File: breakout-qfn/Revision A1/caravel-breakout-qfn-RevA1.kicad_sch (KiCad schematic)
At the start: 14 parts, among them CON1 REF-182665-01, CON2 REF-182665-01, CON3 73251-1352, U1 Caravel, U2 TLV73318PDBV

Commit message: WIP checkin for comments
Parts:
- removed U1: Caravel, ok-chips:Caravel_WLCSP, symbol ok-chips:Caravel_WLCSP
- added U1: Caravel_QFN, Package_DFN_QFN:QFN-64-1EP_9x9mm_P0.5mm_EP7.65x7.65mm, symbol ok-chips:Caravel_QFN
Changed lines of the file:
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@@
     )
-  )
-  (symbol (lib_id "ok-chips:Caravel_WLCSP") (at 93.98 82.55 90) (unit 1)
-    (in_bom yes) (on_board yes)
-    (property "Reference" "U1" (id 0) (at 64.77 54.61 90)
-      (effects (font (size 1.27 1.27)) (justify left))
-    )
-    (property "Value" "Caravel" (id 1) (at 134.62 107.95 90)
-      (effects (font (size 1.27 1.27)) (justify left))
-    )
-    (property "Footprint" "ok-chips:Caravel_WLCSP" (id 2) (at 137.16 54.61 0)
-      (effects (font (size 1.27 1.27)) (justify left) hide)
-    )
-    (property "Datasheet" "" (id 3) (at 93.98 82.55 0)
-      (effects (font (size 1.27 1.27)) hide)
-    )
-    (property "LibSource" "https://github.com/efabless/caravel_board/blob/84c2a618c3ccb63b4e827d80adff53c441349ad6/hardware/symbols/Caravel_board.kicad_sym" (id 4) (at 139.7 54.61 0)
-      (effects (font (size 1.27 1.27)) (justify left) hide)
-    )
-    (pin "A1")
-    (pin "A10")
-    (pin "A2")
-    (pin "A3")
-    (pin "A4")
-    (pin "A5")
-    (pin "A6")
-    (pin "A7")
-    (pin "A8")
-    (pin "A9")
-    (pin "B1")
-    (pin "B10")
-    (pin "B2")
-    (pin "B3")
-    (pin "B4")
-    (pin "B5")
-    (pin "B6")
-    (pin "B7")
-    (pin "B8")
-    (pin "B9")
-    (pin "C1")
-    (pin "C10")
-    (pin "C2")
-    (pin "C3")
-    (pin "C4")
-    (pin "C5")
-    (pin "C6")
-    (pin "C7")
-    (pin "C8")
-    (pin "C9")
-    (pin "D1")
-    (pin "D10")
-    (pin "D2")
-    (pin "D3")
-    (pin "D4")
-    (pin "D5")
-    (pin "D6")
-    (pin "D7")
-    (pin "D8")
-    (pin "D9")
-    (pin "E1")
-    (pin "E10")
-    (pin "E2")
-    (pin "E3")
-    (pin "E4")
-    (pin "E5")
-    (pin "E6")
-    (pin "E7")
-    (pin "E8")
-    (pin "E9")
-    (pin "F1")
-    (pin "F10")
-    (pin "F2")
-    (pin "F3")
-    (pin "F4")
-    (pin "F5")
-    (pin "F6")
-    (pin "F7")
-    (pin "F8")
-    (pin "F9")
   )
   (symbol (lib_id "Device:C") (at 162.56 69.85 0) (unit 1)
@@
     )
     (pin "1")
-  )
-  (symbol (lib_id "Regulator_Linear:TLV73318PDBV") (at 144.78 157.48 0) (unit 1)
-    (in_bom yes) (on_board yes) (fields_autoplaced)
-    (property "Reference" "U2" (id 0) (at 144.78 147.32 0))
-    (property "Value" "TLV73318PDBV" (id 1) (at 144.78 149.86 0))
-    (property "Footprint" "Package_TO_SOT_SMD:SOT-23-5" (id 2) (at 144.78 149.225 0)
-      (effects (font (size 1.27 1.27) italic) hide)
-    )
-    (property "Datasheet" "http://www.ti.com/lit/ds/symlink/tlv733p.pdf" (id 3) (at 144.78 157.48 0)
-      (effects (font (size 1.27 1.27)) hide)
-    )
-    (pin "1")
-    (pin "2")
-    (pin "3")
-    (pin "4")
-    (pin "5")
   )
   (symbol (lib_id "Connector_Generic:Conn_02x20_Odd_Even") (at 222.25 52.07 0) (unit 1)
@@
     (pin "9")
   )
+  (symbol (lib_id "Device:C") (at 161.29 156.21 180) (unit 1)
+    (in_bom yes) (on_board yes)
+    (property "Reference" "C9" (id 0) (at 157.48 156.21 90))
+    (property "Value" "0.1uf" (id 1) (at 154.94 156.21 90))
+    (property "Footprint" "Capacitor_SMD:C_0603_1608Metric" (id 2) (at 160.3248 152.4 0)
+      (effects (font (size 1.27 1.27)) hide)
+    )
+    (property "Datasheet" "~" (id 3) (at 161.29 156.21 0)
+      (effects (font (size 1.27 1.27)) hide)
+    )
+    (pin "1")
+    (pin "2")
+  )
+  (symbol (lib_id "Regulator_Linear:TLV73318PDBV") (at 146.05 154.94 0) (unit 1)
+    (in_bom yes) (on_board yes) (fields_autoplaced)
+    (property "Reference" "U2" (id 0) (at 146.05 144.78 0))
+    (property "Value" "TLV73318PDBV" (id 1) (at 146.05 147.32 0))
+    (property "Footprint" "Package_TO_SOT_SMD:SOT-23-5" (id 2) (at 146.05 146.685 0)
+      (effects (font (size 1.27 1.27) italic) hide)
+    )
+    (property "Datasheet" "http://www.ti.com/lit/ds/symlink/tlv733p.pdf" (id 3) (at 146.05 154.94 0)
+      (effects (font (size 1.27 1.27)) hide)
+    )
+    (pin "1")
+    (pin "2")
+    (pin "3")
+    (pin "4")
+    (pin "5")
+  )
   (symbol (lib_id "power:GND") (at 234.95 81.28 0) (unit 1)
     (in_bom yes) (on_board yes)
@@
     (pin "1")
   )
+  (symbol (lib_id "ok-chips:Caravel_QFN") (at 35.56 175.26 0) (unit 1)
+    (in_bom yes) (on_board yes) (fields_autoplaced)
+    (property "Reference" "U1" (id 0) (at 67.31 145.8212 0))
+    (property "Value" "Caravel_QFN" (id 1) (at 67.31 148.3612 0))
+    (property "Footprint" "Package_DFN_QFN:QFN-64-1EP_9x9mm_P0.5mm_EP7.65x7.65mm" (id 2) (at 60.96 209.55 0)
+      (effects (font (size 1.27 1.27)) (justify left) hide)
+    )
+    (property "Datasheet" "" (id 3) (at 35.56 175.26 0)
+      (effects (font (size 1.27 1.27)) hide)
+    )
+    (property "LibSource" "https://github.com/efabless/caravel_board/blob/84c2a618c3ccb63b4e827d80adff53c441349ad6/hardware/symbols/Caravel_board.kicad_sym" (id 4) (at 60.96 212.09 0)
+      (effects (font (size 1.27 1.27)) (justify left) hide)
+    )
+    (pin "1")
+    (pin "10")
+    (pin "11")
+    (pin "12")
+    (pin "13")
+    (pin "14")
+    (pin "15")
+    (pin "16")
+    (pin "17")
+    (pin "18")
+    (pin "19")
+    (pin "2")
+    (pin "20")
+    (pin "21")
+    (pin "22")
+    (pin "23")
+    (pin "24")
+    (pin "25")
+    (pin "26")
+    (pin "27")
+    (pin "28")
+    (pin "29")
+    (pin "3")
+    (pin "30")
+    (pin "31")
+    (pin "32")
+    (pin "33")
+    (pin "34")
+    (pin "35")
+    (pin "36")
+    (pin "37")
+    (pin "38")
+    (pin "39")
+    (pin "4")
+    (pin "40")
+    (pin "41")
+    (pin "42")
+    (pin "43")
+    (pin "44")
+    (pin "45")
+    (pin "46")
+    (pin "47")
+    (pin "48")
+    (pin "49")
+    (pin "5")
+    (pin "50")
+    (pin "51")
+    (pin "52")
+    (pin "53")
+    (pin "54")
+    (pin "55")
+    (pin "56")
+    (pin "57")
+    (pin "58")
+    (pin "59")
+    (pin "6")
+    (pin "60")
+    (pin "61")
+    (pin "62")
+    (pin "63")
+    (pin "64")
+    (pin "65")
+    (pin "7")
+    (pin "8")
+    (pin "9")
+  )
   (symbol (lib_id "power:GND") (at 212.09 81.28 0) (unit 1)
     (in_bom yes) (on_board yes)
@@
     (pin "1")
   )
-  (symbol (lib_id "Device:C") (at 129.54 158.75 180) (unit 1)
-    (in_bom yes) (on_board yes)
-    (property "Reference" "C8" (id 0) (at 125.73 158.75 90))
-    (property "Value" "0.1uf" (id 1) (at 123.19 158.75 90))
-    (property "Footprint" "Capacitor_SMD:C_0603_1608Metric" (id 2) (at 128.5748 154.94 0)
-      (effects (font (size 1.27 1.27)) hide)
-    )
-    (property "Datasheet" "~" (id 3) (at 129.54 158.75 0)
-      (effects (font (size 1.27 1.27)) hide)
-    )
-    (pin "1")
-    (pin "2")
-  )
   (symbol (lib_id "power:GND") (at 212.09 154.94 0) (unit 1)
     (in_bom yes) (on_board yes)
@@
     (pin "1")
   )
-  (symbol (lib_id "Device:C") (at 160.02 158.75 180) (unit 1)
-    (in_bom yes) (on_board yes)
-    (property "Reference" "C9" (id 0) (at 156.21 158.75 90))
-    (property "Value" "0.1uf" (id 1) (at 153.67 158.75 90))
-    (property "Footprint" "Capacitor_SMD:C_0603_1608Metric" (id 2) (at 159.0548 154.94 0)
-      (effects (font (size 1.27 1.27)) hide)
-    )
-    (property "Datasheet" "~" (id 3) (at 160.02 158.75 0)
+  (symbol (lib_id "Device:C") (at 130.81 156.21 180) (unit 1)
+    (in_bom yes) (on_board yes)
+    (property "Reference" "C8" (id 0) (at 127 156.21 90))
+    (property "Value" "0.1uf" (id 1) (at 124.46 156.21 90))
+    (property "Footprint" "Capacitor_SMD:C_0603_1608Metric" (id 2) (at 129.8448 152.4 0)
+      (effects (font (size 1.27 1.27)) hide)
+    )
+    (property "Datasheet" "~" (id 3) (at 130.81 156.21 0)
       (effects (font (size 1.27 1.27)) hide)
     )
@@
       (reference "C7") (unit 1) (value "0.1uf") (footprint "Capacitor_SMD:C_0402_1005Metric")
     )
-    (path "/748e673c-62ba-48f2-8c93-fcf00774af87"
+    (path "/a1f5d155-7c5b-450f-835a-1beaa84985c2"
       (reference "C8") (unit 1) (value "0.1uf") (footprint "Capacitor_SMD:C_0603_1608Metric")
     )
-    (path "/9c14b6d3-b2f0-4fdc-9232-d4338971c346"
+    (path "/490fa7a0-dc17-4ffe-be30-513cc3f5aca8"
       (reference "C9") (unit 1) (value "0.1uf") (footprint "Capacitor_SMD:C_0603_1608Metric")
     )
@@
       (reference "CON3") (unit 1) (value "73251-1352") (footprint "ok-connectors:TE_5-1814832-2")
     )
-    (path "/00000000-0000-0000-0000-0000612e097b"
-      (reference "U1") (unit 1) (value "Caravel") (footprint "ok-chips:Caravel_WLCSP")
-    )
-    (path "/0d29bb03-4b1f-4213-ba3c-74ea953f1fc4"
+    (path "/629c3e8d-0778-4ca7-bedf-2cc0e61e7e2f"
+      (reference "U1") (unit 1) (value "Caravel_QFN") (footprint "Package_DFN_QFN:QFN-64-1EP_9x9mm_P0.5mm_EP7.65x7.65mm")
+    )
+    (path "/54c9bf1d-870a-4c32-88f6-52ae382a86f1"
       (reference "U2") (unit 1) (value "TLV73318PDBV") (footprint "Package_TO_SOT_SMD:SOT-23-5")
     )

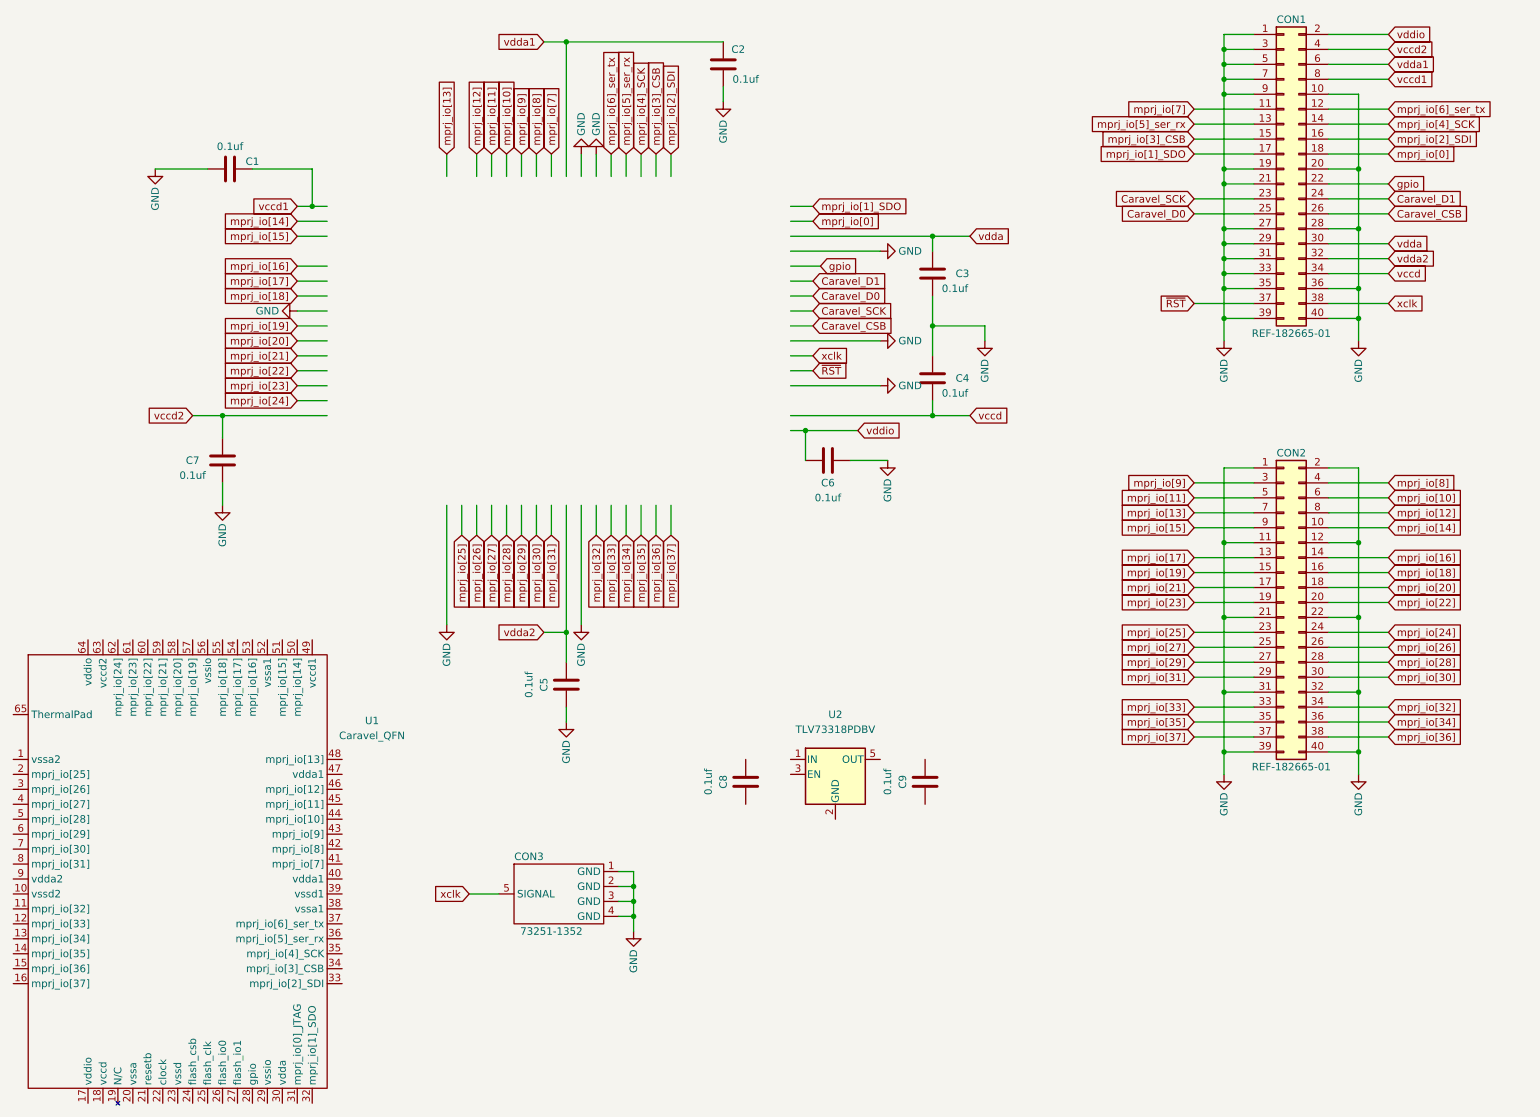
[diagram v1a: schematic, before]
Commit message: kicad 7 migration, qfn symbol and wiring
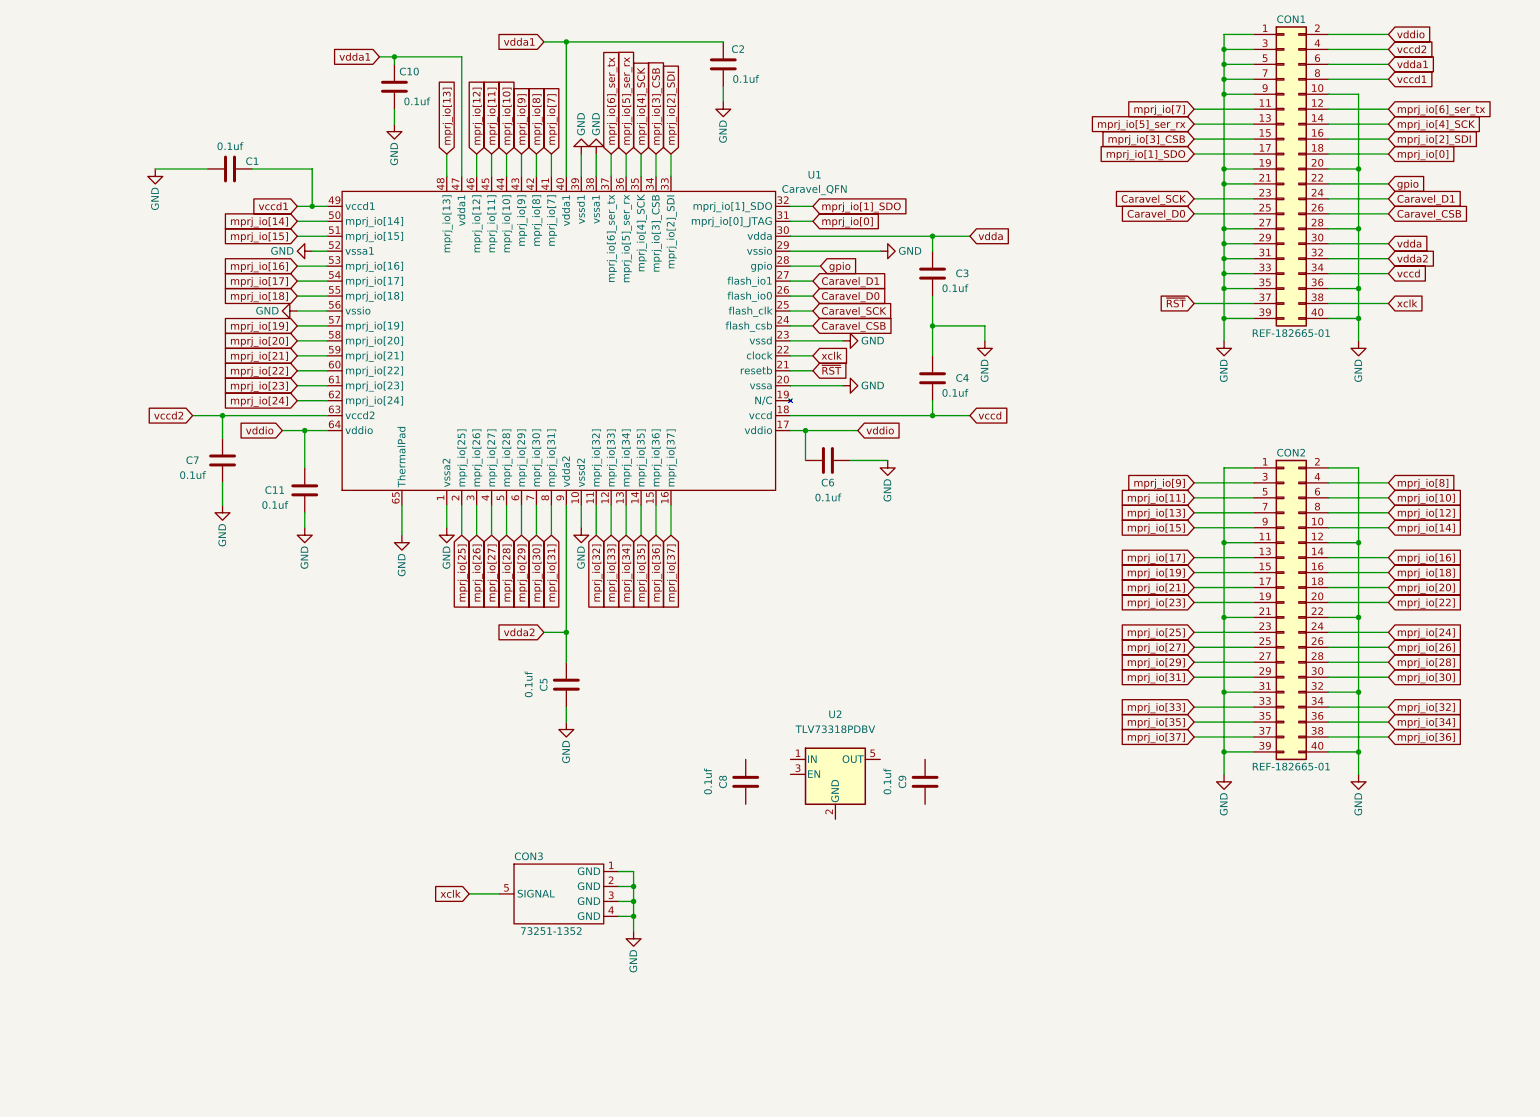
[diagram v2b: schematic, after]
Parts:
- removed U1: Caravel_QFN, Package_DFN_QFN:QFN-64-1EP_9x9mm_P0.5mm_EP7.65x7.65mm, symbol ok-chips:Caravel_QFN
- added C10, C11: 0.1uf, Capacitor_SMD:C_0402_1005Metric, symbol Device:C
- added U1: Caravel_QFN, Package_DFN_QFN:QFN-64-1EP_9x9mm_P0.5mm_EP7.65x7.65mm, symbol CaravelCommon:Caravel_QFN
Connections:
- net Caravel_CSB: now also U1.24 (flash_csb)
- net Caravel_D0: now also U1.26 (flash_io0)
- net Caravel_D1: now also U1.27 (flash_io1)
- net Caravel_SCK: now also U1.25 (flash_clk)
- net GND: now also C10.2, C11.1, U1.1 (vssa2), U1.10 (vssd2), U1.20 (vssa), U1.23 (vssd), U1.29 (vssio), U1.38 (vssa1), U1.39 (vssd1), U1.52 (vssa1), U1.56 (vssio), U1.65 (ThermalPad)
- net gpio: now also U1.28 (gpio)
- net mprj_io[0]: now also U1.31 (mprj_io[0]_JTAG)
- net mprj_io[10]: now also U1.44 (mprj_io[10])
- net mprj_io[11]: now also U1.45 (mprj_io[11])
- net mprj_io[12]: now also U1.46 (mprj_io[12])
- net mprj_io[13]: now also U1.48 (mprj_io[13])
- net mprj_io[14]: now also U1.50 (mprj_io[14])
- net mprj_io[15]: now also U1.51 (mprj_io[15])
- net mprj_io[16]: now also U1.53 (mprj_io[16])
- net mprj_io[17]: now also U1.54 (mprj_io[17])
- net mprj_io[18]: now also U1.55 (mprj_io[18])
- net mprj_io[19]: now also U1.57 (mprj_io[19])
- net mprj_io[1]_SDO: now also U1.32 (mprj_io[1]_SDO)
- net mprj_io[20]: now also U1.58 (mprj_io[20])
- net mprj_io[21]: now also U1.59 (mprj_io[21])
- net mprj_io[22]: now also U1.60 (mprj_io[22])
- net mprj_io[23]: now also U1.61 (mprj_io[23])
- net mprj_io[24]: now also U1.62 (mprj_io[24])
- net mprj_io[25]: now also U1.2 (mprj_io[25])
- net mprj_io[26]: now also U1.3 (mprj_io[26])
- net mprj_io[27]: now also U1.4 (mprj_io[27])
- net mprj_io[28]: now also U1.5 (mprj_io[28])
- net mprj_io[29]: now also U1.6 (mprj_io[29])
- net mprj_io[2]_SDI: now also U1.33 (mprj_io[2]_SDI)
- net mprj_io[30]: now also U1.7 (mprj_io[30])
- net mprj_io[31]: now also U1.8 (mprj_io[31])
- net mprj_io[32]: now also U1.11 (mprj_io[32])
- net mprj_io[33]: now also U1.12 (mprj_io[33])
- net mprj_io[34]: now also U1.13 (mprj_io[34])
- net mprj_io[35]: now also U1.14 (mprj_io[35])
- net mprj_io[36]: now also U1.15 (mprj_io[36])
- net mprj_io[37]: now also U1.16 (mprj_io[37])
- net mprj_io[3]_CSB: now also U1.34 (mprj_io[3]_CSB)
- net mprj_io[4]_SCK: now also U1.35 (mprj_io[4]_SCK)
- net mprj_io[5]_ser_rx: now also U1.36 (mprj_io[5]_ser_rx)
- net mprj_io[6]_ser_tx: now also U1.37 (mprj_io[6]_ser_tx)
- net mprj_io[7]: now also U1.41 (mprj_io[7])
- net mprj_io[8]: now also U1.42 (mprj_io[8])
- net mprj_io[9]: now also U1.43 (mprj_io[9])
- net vccd: now also U1.18 (vccd)
- net vccd1: now also U1.49 (vccd1)
- net vccd2: now also U1.63 (vccd2)
- net vdda: now also U1.30 (vdda)
- net vdda1: now also C10.1, U1.40 (vdda1), U1.47 (vdda1)
- net vdda2: now also U1.9 (vdda2)
- net vddio: now also C11.2, U1.17 (vddio), U1.64 (vddio)
- net xclk: now also U1.22 (clock)
- net ~{RST}: now also U1.21 (resetb)
